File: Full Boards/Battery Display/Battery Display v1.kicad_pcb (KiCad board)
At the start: 4 copper layers, 110 x 175.2 mm, 195 parts, among them J2 Program Header, Q1 AO3401A, Q2 2N3904, Q3 AO3401A, Q4 2N3904, Q5 AO3401A, Q6 2N3904, SW1 SW_MEC_5G, SW2 SW_MEC_5G, U1 ISO1044BD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

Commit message: Updated PCBs to swap RVS diodes from SLD15-018 to SLD22-018. Also swapped out the inductor from 7847111100 to PA4340.103NLT.
Signed-off-by: Madison Kelly <digital.mermaid@gmail.com>
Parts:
- D146: value SLD15-018 -> SLD22-018
- L1: value 7847111100 -> PA4340.103NLT; footprint mr-stuff:WE-RCIT_7847111100 -> mr-stuff:Pulse PA4340.103NLT
- moved L1 3.27 mm to (61.0, 37.5), turned to 90 degrees
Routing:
- net V_RAW: track 134.7 -> 139.5 mm, vias 0 -> 1
- net Net-(PS1-+VIN): track 40.2 -> 39.6 mm

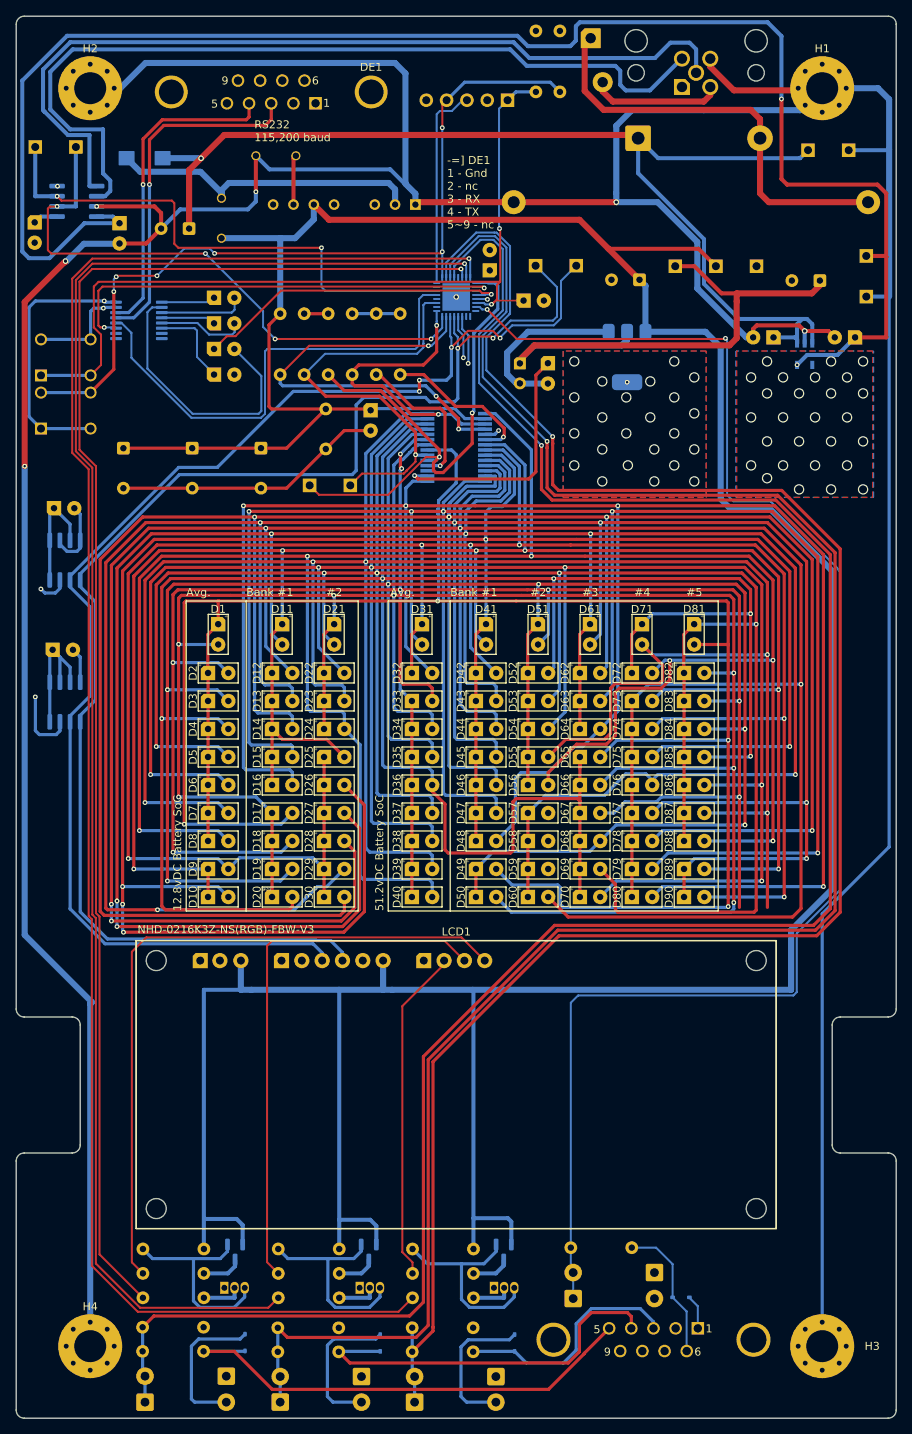
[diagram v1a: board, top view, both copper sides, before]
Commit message: Updated boards and schematics.
These are the version that have been ordered. Any further changes will be a new version.

Signed-off-by: Madison Kelly <digital.mermaid@gmail.com>
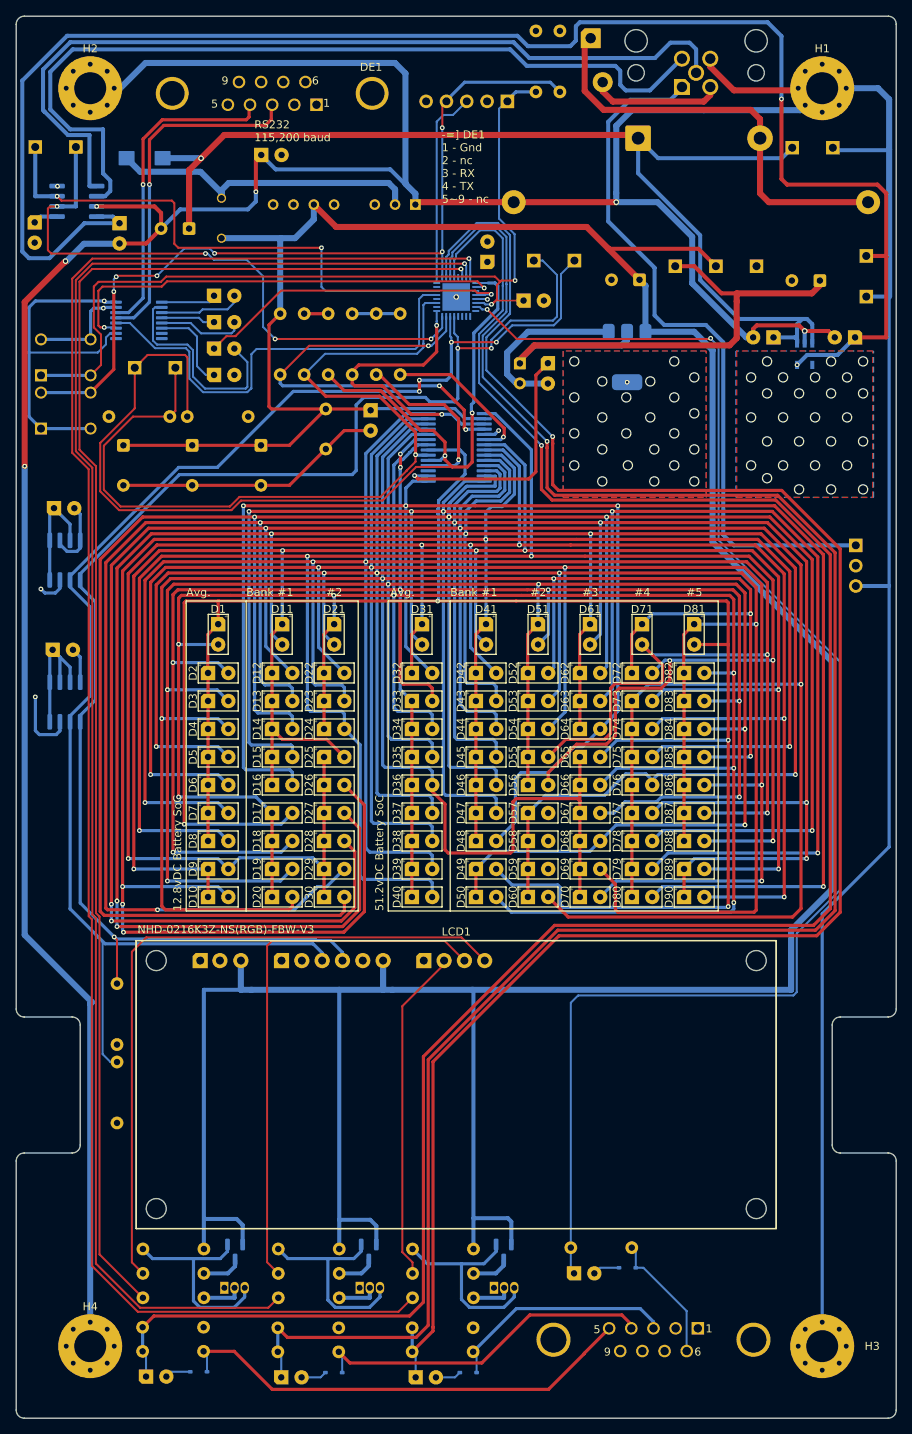
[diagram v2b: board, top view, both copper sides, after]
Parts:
- removed D100, D101, D102, D103, D104, D105, D106, D107: 1N5822, Diode_THT:D_DO-41_SOD81_P10.16mm_Horizontal
- added C25: 0.1uF, mr-stuff:RCE5C1H104J2A2H03B, B.Cu at (115.9, 176.9)
- added C26: 0.1uF, mr-stuff:RCE5C1H104J2A2H03B, B.Cu at (62.4, 189.8)
- added C27: 0.1uF, mr-stuff:RCE5C1H104J2A2H03B, B.Cu at (79.3, 189.9)
- added C28: 0.1uF, mr-stuff:RCE5C1H104J2A2H03B, B.Cu at (96.1, 189.9)
- added J1: Future Bonding, Connector_PinHeader_2.54mm:PinHeader_1x03_P2.54mm_Horizontal, B.Cu at (149.8, 85.9)
- added R24: 3.3K, Resistor_THT:R_Axial_DIN0207_L6.3mm_D2.5mm_P7.62mm_Horizontal, B.Cu at (73.9, 69.8)
- added R25: 3.3K, Resistor_THT:R_Axial_DIN0207_L6.3mm_D2.5mm_P7.62mm_Horizontal, B.Cu at (56.5, 69.8)
- added R26: 3.3K, Resistor_THT:R_Axial_DIN0207_L6.3mm_D2.5mm_P7.62mm_Horizontal, B.Cu at (57.5, 148.3)
- added R27: 3.3K, Resistor_THT:R_Axial_DIN0207_L6.3mm_D2.5mm_P7.62mm_Horizontal, B.Cu at (57.5, 158.1)
- C5: value TDK FA28NP01H152JNU06 -> 0.1uF; footprint mr-stuff:TDK CAPRB500W50L400T250H550 -> mr-stuff:RCE5C1H104J2A2H03B
- R21, R22, R23, R89: value 10 -> 475
- moved TP10 26.3 mm to (59.7, 63.7)
- moved TP11 26.3 mm to (64.8, 63.7)
- moved TVS1 7.65 mm to (121.3, 176.2), turned to 180 degrees
- moved TVS3 6.88 mm to (84.6, 189.3), turned to 180 degrees
- moved TVS4 6.88 mm to (101.4, 189.3), turned to 180 degrees
- moved TVS2 6.85 mm to (67.7, 189.2), turned to 180 degrees
- moved TP2 2.00 mm to (147.0, 36.2)
- moved TP1 2.00 mm to (141.9, 36.2)
- moved C11 1.10 mm to (103.8, 49.2)
- moved TP12 0.68 mm to (109.6, 50.3)
- moved TP13 0.68 mm to (114.7, 50.3)
- moved C5 0.57 mm to (76.8, 37.1), turned to 0 degrees
- moved C13 0.36 mm to (75.5, 73.4)
- moved C14 0.36 mm to (66.9, 73.4)
- moved C15 0.36 mm to (58.3, 73.4)
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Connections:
- C5 pad 1: GND -> GND_SHIP
- C5 pad 2: GND_SHIP -> GND
- N2K1 pad 1: unconnected-(N2K1-Shield-Pad1) -> Net-(J1-Pin_1)
- U5 pad 10: unconnected-(U5-T2IN-Pad10) -> +3.3V
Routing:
- net Net-(J1-Pin_1): track 0.00 -> 88.9 mm
- net /IS31_I2C_SDA: track 71.4 -> 132.4 mm
- net /IS31_I2C_SCL: track 54.9 -> 110.1 mm
- net GND: track 169.7 -> 117.4 mm
- net /BOARD_I2C_SCL: track 168.1 -> 183.9 mm
- net /CA3: track 255.7 -> 241.7 mm
- net +3.3V: track 181.7 -> 194.1 mm
- net /CA8: track 300.8 -> 289.0 mm
- net Net-(U5-VS+): track 35.0 -> 26.9 mm
- net /BRIGHTNESS_POT_IN: track 191.4 -> 184.5 mm
- net /BOARD_I2C_SDA: track 173.4 -> 180.2 mm, vias 2 -> 3
- net unconnected-(U3-PA4-Pad11): track 6.20 -> 0.00 mm, vias 1 -> 0
- net GND_SHIP: track 558.8 -> 564.8 mm
- net unconnected-(U3-PA5-Pad12): track 5.43 -> 0.00 mm, vias 1 -> 0
- net /LCD_PGDOWN_IN_PLUG: track 48.6 -> 43.5 mm
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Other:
- board text added: "Board SCL"
- board text added: "Board SDA"
- board text added: "IS31 SCL"
- board text added: "IS31 SDA"
- board text removed: "BOARD_SCL"
- board text removed: "BOARD_SDA"
- board text removed: "IS31_SCL"
- board text removed: "IS31_SDA"
